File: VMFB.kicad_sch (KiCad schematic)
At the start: 111 parts, among them J1 Barrel_Jack_Switch, J10 Conn_01x03_Pin, J11 Conn_01x08_Pin, J12 Conn_01x04_Pin, J13 Conn_01x04_Pin, J14 Conn_01x04_Pin, J2 USB_B, J3 Screw_Terminal_01x02, J4 Screw_Terminal_01x03, J5 Conn_01x03_Pin, J6 Conn_01x04_Pin, J7 Conn_01x04_Pin, J8 Conn_01x04_Pin, J9 Conn_01x02_Pin, Q1 BC547, Q2 BC547, Q3 BC547, Q4 BD139, Q5 TIP41C, Q6 BC547, U1 LM358, U2 NE555P, U3 NE555P, U4 NE555P, U5 NE555P

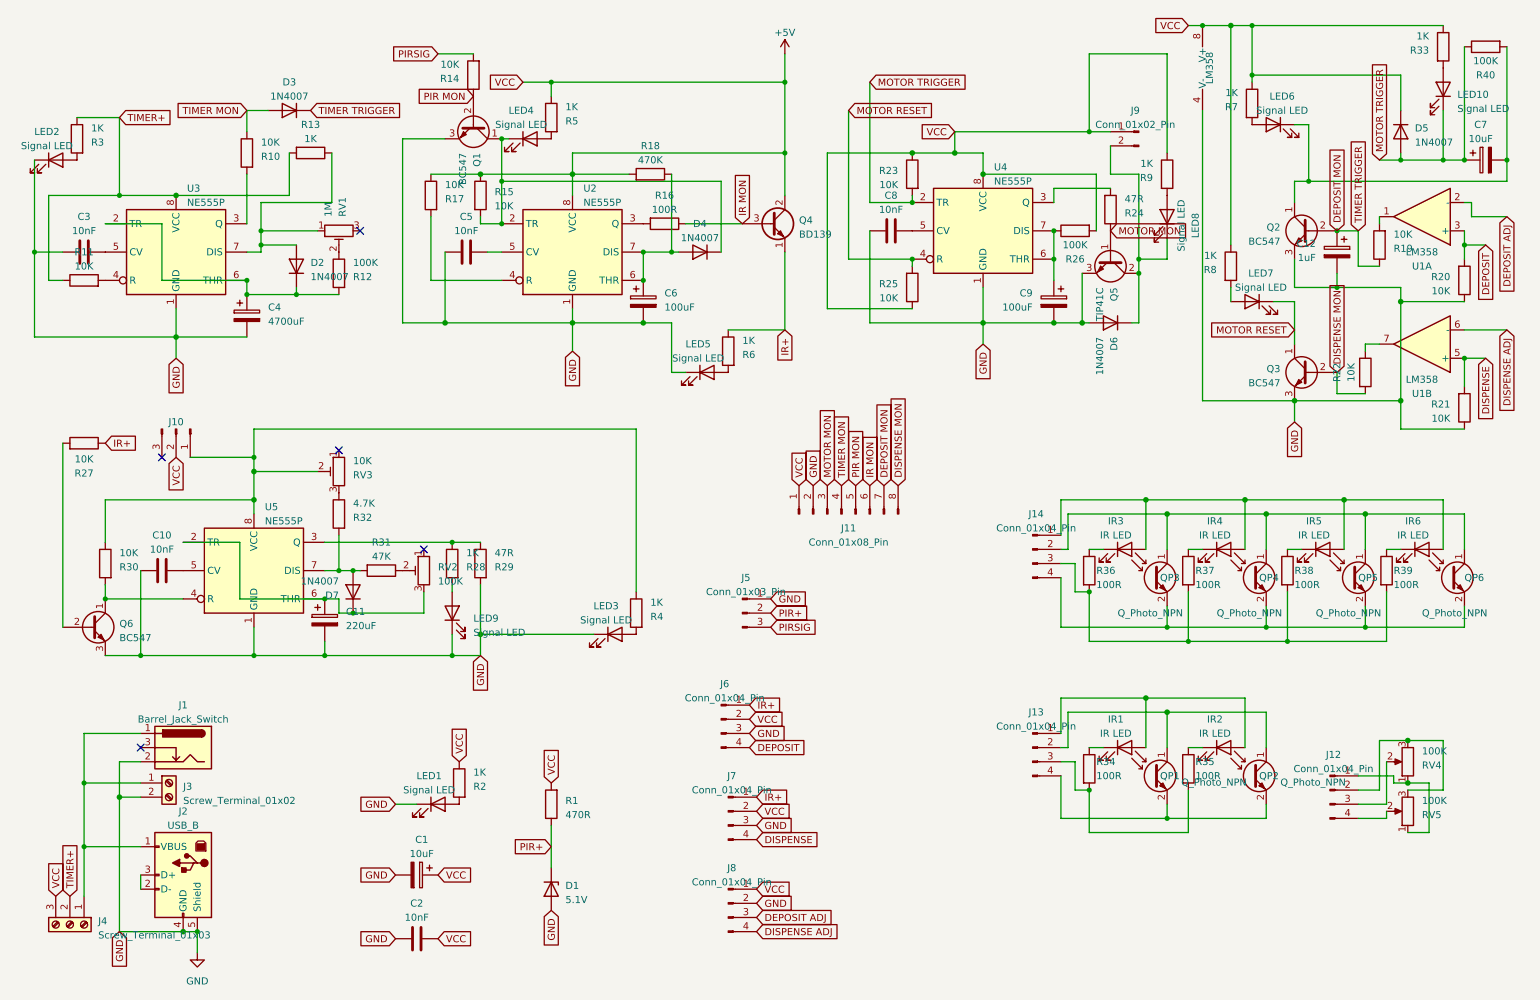
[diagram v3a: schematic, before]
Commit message: changed external header to 6-pin with pinout to match most 4-channel level shifters, removed 2 unnecessary 10K reset resistors from timer and IR power 555s
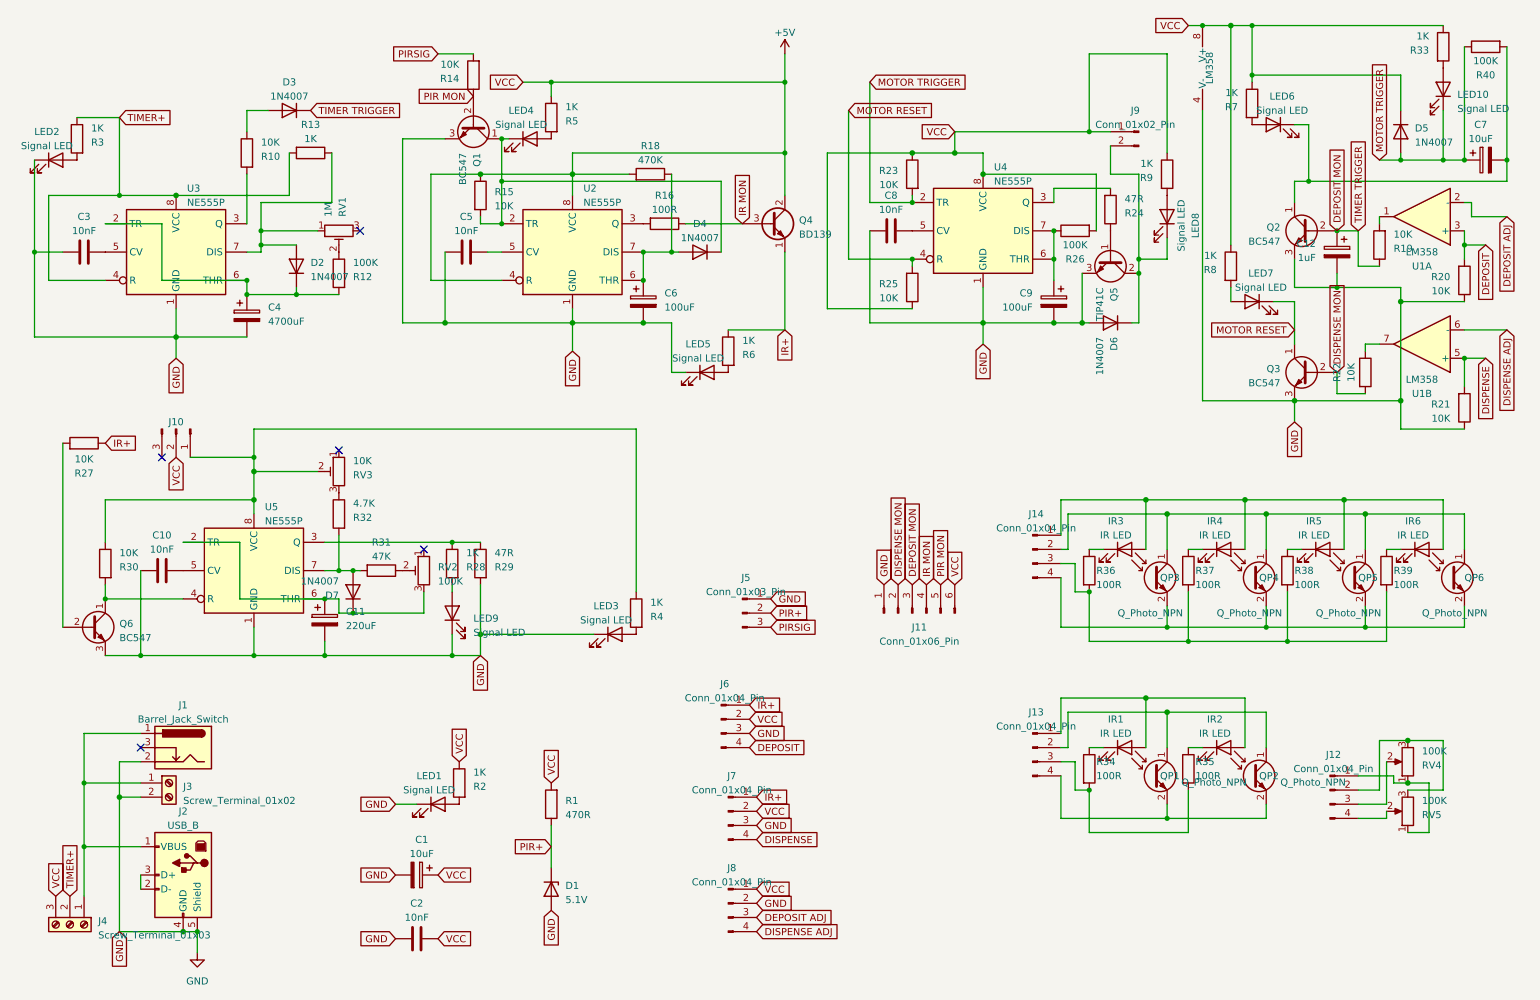
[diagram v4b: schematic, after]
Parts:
- removed J11: Conn_01x08_Pin, Connector_PinHeader_2.54mm:PinHeader_1x08_P2.54mm_Vertical, symbol Connector:Conn_01x08_Pin
- removed R11, R17: 10K, Resistor_THT:R_Axial_DIN0207_L6.3mm_D2.5mm_P2.54mm_Vertical, symbol Device:R
- added J11: Conn_01x06_Pin, Connector_PinHeader_2.54mm:PinHeader_1x06_P2.54mm_Vertical, symbol Connector:Conn_01x06_Pin
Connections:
- net +5V: now also U2.4 (R), J11.6 (Pin_6)
- net DEPOSIT MON: now also J11.3 (Pin_3)
- net DISPENSE MON: now also J11.2 (Pin_2)
- net GND: now also J11.1 (Pin_1)
- net IR MON: now also J11.4 (Pin_4)
- net PIR MON: now also J11.5 (Pin_5)
- net TIMER+: now also U3.4 (R)
- net MOTOR MON: no longer names the net of Q5.1 (B), R24.1
- net TIMER MON: no longer names the net of D3.2 (A), R10.1
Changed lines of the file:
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@@
     (stroke (width 0) (type default) (color 153 12 207 1))
   )
-  (wire (pts (xy 88.9 52.07) (xy 88.9 63.5))
-    (stroke (width 0) (type default))
-  )
   (wire (pts (xy 262.89 90.17) (xy 262.89 85.09))
     (stroke (width 0) (type default) (color 0 0 0 1))
@@
     (stroke (width 0) (type default))
   )
-  (wire (pts (xy 20.32 63.5) (xy 22.86 63.5))
+  (wire (pts (xy 20.32 63.5) (xy 30.48 63.5))
     (stroke (width 0) (type default) (color 255 221 0 1))
   )
@@
     (stroke (width 0) (type default))
   )
+  (wire (pts (xy 88.9 63.5) (xy 101.6 63.5))
+    (stroke (width 0) (type default) (color 194 0 0 1))
+  )
   (wire (pts (xy 110.49 27.94) (xy 110.49 30.48))
     (stroke (width 0) (type default) (color 194 0 0 1))
@@
     (stroke (width 0) (type default) (color 255 0 0 1))
   )
-  (wire (pts (xy 88.9 63.5) (xy 101.6 63.5))
-    (stroke (width 0) (type default))
-  )
   (wire (pts (xy 127 58.42) (xy 132.08 58.42))
     (stroke (width 0) (type default))
@@
     (stroke (width 0) (type default) (color 0 0 0 1))
   )
+  (wire (pts (xy 88.9 44.45) (xy 88.9 63.5))
+    (stroke (width 0) (type default) (color 194 0 0 1))
+  )
   (wire (pts (xy 87.63 119.38) (xy 87.63 123.19))
     (stroke (width 0) (type default))
@@
     )
   )
-  (global_label "GND" (shape input) (at 157.48 100.33 90) (fields_autoplaced)
+  (global_label "GND" (shape input) (at 170.18 118.11 90) (fields_autoplaced)
     (effects (font (size 1.27 1.27)) (justify left))
-    (property "Intersheetrefs" "${INTERSHEET_REFS}" (at 157.48 93.5537 90) (show_name)
+    (property "Intersheetrefs" "${INTERSHEET_REFS}" (at 170.18 111.3337 90) (show_name)
       (effects (font (size 1.27 1.27)) (justify left) hide)
     )
@@
     )
   )
-  (global_label "PIR MON" (shape input) (at 165.1 100.33 90) (fields_autoplaced)
+  (global_label "PIR MON" (shape input) (at 180.34 118.11 90) (fields_autoplaced)
     (effects (font (size 1.27 1.27)) (justify left))
-    (property "Intersheetrefs" "${INTERSHEET_REFS}" (at 165.1 89.1994 90) (show_name)
+    (property "Intersheetrefs" "${INTERSHEET_REFS}" (at 180.34 106.9794 90) (show_name)
       (effects (font (size 1.27 1.27)) (justify left) hide)
     )
@@
     )
   )
-  (global_label "TIMER MON" (shape input) (at 55.88 33.02 180) (fields_autoplaced)
-    (effects (font (size 1.27 1.27)) (justify right))
-    (property "Intersheetrefs" "${INTERSHEET_REFS}" (at 42.4514 33.02 0) (show_name)
-      (effects (font (size 1.27 1.27)) (justify right) hide)
-    )
-  )
   (global_label "GND" (shape input) (at 146.05 144.78 0) (fields_autoplaced)
     (effects (font (size 1.27 1.27)) (justify left))
@@
     )
   )
-  (global_label "VCC" (shape input) (at 154.94 100.33 90) (fields_autoplaced)
+  (global_label "VCC" (shape input) (at 182.88 118.11 90) (fields_autoplaced)
     (effects (font (size 1.27 1.27)) (justify left))
-    (property "Intersheetrefs" "${INTERSHEET_REFS}" (at 154.94 93.7956 90) (show_name)
+    (property "Intersheetrefs" "${INTERSHEET_REFS}" (at 182.88 111.5756 90) (show_name)
       (effects (font (size 1.27 1.27)) (justify left) hide)
     )
@@
     )
   )
-  (global_label "DEPOSIT MON" (shape input) (at 170.18 100.33 90) (fields_autoplaced)
+  (global_label "DEPOSIT MON" (shape input) (at 175.26 118.11 90) (fields_autoplaced)
     (effects (font (size 1.27 1.27)) (justify left))
-    (property "Intersheetrefs" "${INTERSHEET_REFS}" (at 170.18 84.5428 90) (show_name)
+    (property "Intersheetrefs" "${INTERSHEET_REFS}" (at 175.26 102.3228 90) (show_name)
       (effects (font (size 1.27 1.27)) (justify left) hide)
     )
@@
     )
   )
-  (global_label "MOTOR MON" (shape input) (at 210.82 54.61 0) (fields_autoplaced)
-    (effects (font (size 1.27 1.27)) (justify left))
-    (property "Intersheetrefs" "${INTERSHEET_REFS}" (at 225.1558 54.61 0) (show_name)
-      (effects (font (size 1.27 1.27)) (justify left) hide)
-    )
-  )
   (global_label "MOTOR TRIGGER" (shape input) (at 167.64 27.94 0) (fields_autoplaced)
     (effects (font (size 1.27 1.27)) (justify left))
@@
     )
   )
-  (global_label "MOTOR MON" (shape input) (at 160.02 100.33 90) (fields_autoplaced)
-    (effects (font (size 1.27 1.27)) (justify left))
-    (property "Intersheetrefs" "${INTERSHEET_REFS}" (at 160.02 85.9942 90) (show_name)
-      (effects (font (size 1.27 1.27)) (justify left) hide)
-    )
-  )
   (global_label "IR+" (shape input) (at 146.05 139.7 0) (fields_autoplaced)
     (effects (font (size 1.27 1.27)) (justify left))
@@
     )
   )
-  (global_label "IR MON" (shape input) (at 167.64 100.33 90) (fields_autoplaced)
+  (global_label "IR MON" (shape input) (at 177.8 118.11 90) (fields_autoplaced)
     (effects (font (size 1.27 1.27)) (justify left))
-    (property "Intersheetrefs" "${INTERSHEET_REFS}" (at 167.64 90.4694 90) (show_name)
-      (effects (font (size 1.27 1.27)) (justify left) hide)
-    )
-  )
-  (global_label "TIMER MON" (shape input) (at 162.56 100.33 90) (fields_autoplaced)
-    (effects (font (size 1.27 1.27)) (justify left))
-    (property "Intersheetrefs" "${INTERSHEET_REFS}" (at 162.56 86.9014 90) (show_name)
+    (property "Intersheetrefs" "${INTERSHEET_REFS}" (at 177.8 108.2494 90) (show_name)
       (effects (font (size 1.27 1.27)) (justify left) hide)
     )
@@
     )
   )
-  (global_label "DISPENSE MON" (shape input) (at 172.72 100.33 90) (fields_autoplaced)
+  (global_label "DISPENSE MON" (shape input) (at 172.72 118.11 90) (fields_autoplaced)
     (effects (font (size 1.27 1.27)) (justify left))
-    (property "Intersheetrefs" "${INTERSHEET_REFS}" (at 172.72 83.1519 90) (show_name)
+    (property "Intersheetrefs" "${INTERSHEET_REFS}" (at 172.72 100.9319 90) (show_name)
       (effects (font (size 1.27 1.27)) (justify left) hide)
     )
@@
     )
   )
-  (symbol (lib_id "Connector:Conn_01x08_Pin") (at 162.56 105.41 90) (unit 1)
-    (in_bom yes) (on_board yes) (dnp no) (fields_autoplaced)
-    (property "Reference" "J11" (at 163.83 107.95 90)
-      (effects (font (size 1.27 1.27)))
-    )
-    (property "Value" "Conn_01x08_Pin" (at 163.83 110.49 90)
-      (effects (font (size 1.27 1.27)))
-    )
-    (property "Footprint" "Connector_PinHeader_2.54mm:PinHeader_1x08_P2.54mm_Vertical" (at 162.56 105.41 0)
-      (effects (font (size 1.27 1.27)) hide)
-    )
-    (property "Datasheet" "~" (at 162.56 105.41 0)
-      (effects (font (size 1.27 1.27)) hide)
-    )
-    (pin "1")
-    (pin "2")
-    (pin "3")
-    (pin "4")
-    (pin "5")
-    (pin "6")
-    (pin "7")
-    (pin "8")
-    (instances
-      (project "VMFB"
-        (path "/840789ee-60d4-4003-8113-c1b030a45492"
-          (reference "J11") (unit 1)
-        )
-      )
-    )
-  )
   (symbol (lib_id "Device:Q_Photo_NPN") (at 236.22 116.84 0) (unit 1)
     (in_bom yes) (on_board yes) (dnp no)
@@
     )
   )
-  (symbol (lib_id "Device:R") (at 26.67 63.5 90) (unit 1)
-    (in_bom yes) (on_board yes) (dnp no)
-    (property "Reference" "R11" (at 26.67 58.42 90)
-      (effects (font (size 1.27 1.27)))
-    )
-    (property "Value" "10K" (at 26.67 60.96 90)
-      (effects (font (size 1.27 1.27)))
-    )
-    (property "Footprint" "Resistor_THT:R_Axial_DIN0207_L6.3mm_D2.5mm_P2.54mm_Vertical" (at 26.67 65.278 90)
-      (effects (font (size 1.27 1.27)) hide)
-    )
-    (property "Datasheet" "~" (at 26.67 63.5 0)
-      (effects (font (size 1.27 1.27)) hide)
-    )
-    (pin "1")
-    (pin "2")
-    (instances
-      (project "VMFB"
-        (path "/840789ee-60d4-4003-8113-c1b030a45492"
-          (reference "R11") (unit 1)
-        )
-      )
-    )
-  )
   (symbol (lib_id "Device:R") (at 224.79 151.13 0) (unit 1)
     (in_bom yes) (on_board yes) (dnp no)
@@
     )
   )
+  (symbol (lib_id "Connector:Conn_01x06_Pin") (at 175.26 123.19 90) (unit 1)
+    (in_bom yes) (on_board yes) (dnp no) (fields_autoplaced)
+    (property "Reference" "J11" (at 176.53 125.73 90)
+      (effects (font (size 1.27 1.27)))
+    )
+    (property "Value" "Conn_01x06_Pin" (at 176.53 128.27 90)
+      (effects (font (size 1.27 1.27)))
+    )
+    (property "Footprint" "Connector_PinHeader_2.54mm:PinHeader_1x06_P2.54mm_Vertical" (at 175.26 123.19 0)
+      (effects (font (size 1.27 1.27)) hide)
+    )
+    (property "Datasheet" "~" (at 175.26 123.19 0)
+      (effects (font (size 1.27 1.27)) hide)
+    )
+    (pin "1")
+    (pin "2")
+    (pin "3")
+    (pin "4")
+    (pin "5")
+    (pin "6")
+    (instances
+      (project "VMFB"
+        (path "/840789ee-60d4-4003-8113-c1b030a45492"
+          (reference "J11") (unit 1)
+        )
+      )
+    )
+  )
   (symbol (lib_id "Device:LED") (at 240.03 35.56 0) (mirror y) (unit 1)
     (in_bom yes) (on_board yes) (dnp no) (fields_autoplaced)
@@
         )
       )
-    )
-  )
-  (symbol (lib_id "Device:R") (at 88.9 48.26 0) (mirror y) (unit 1)
-    (in_bom yes) (on_board yes) (dnp no)
-    (property "Reference" "R17" (at 91.44 48.895 0)
-      (effects (font (size 1.27 1.27)) (justify right))
-    )
-    (property "Value" "10K" (at 91.44 46.355 0)
-      (effects (font (size 1.27 1.27)) (justify right))
-    )
-    (property "Footprint" "Resistor_THT:R_Axial_DIN0207_L6.3mm_D2.5mm_P2.54mm_Vertical" (at 90.678 48.26 90)
-      (effects (font (size 1.27 1.27)) hide)
-    )
-    (property "Datasheet" "~" (at 88.9 48.26 0)
-      (effects (font (size 1.27 1.27)) hide)
-    )
-    (pin "1")
-    (pin "2")
-    (instances
-      (project "VMFB"
-        (path "/840789ee-60d4-4003-8113-c1b030a45492"
-          (reference "R17") (unit 1)
-        )
-      )
